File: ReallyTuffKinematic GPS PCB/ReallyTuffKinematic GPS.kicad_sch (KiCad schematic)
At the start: 71 parts, among them IC1 PNT-SG3FS-TR, J1 Conn_01x05_Pin, J2 Conn_01x06_Pin, SW2 SKRPACE010, SW3 SKRPACE010, U1 ESP32-C3-MINI-1-N4, U2 TP4056-42-ESOP8, U3 AP2112K-3.3, U4 DW03C_C41367942, X1 X322512MSB4SI

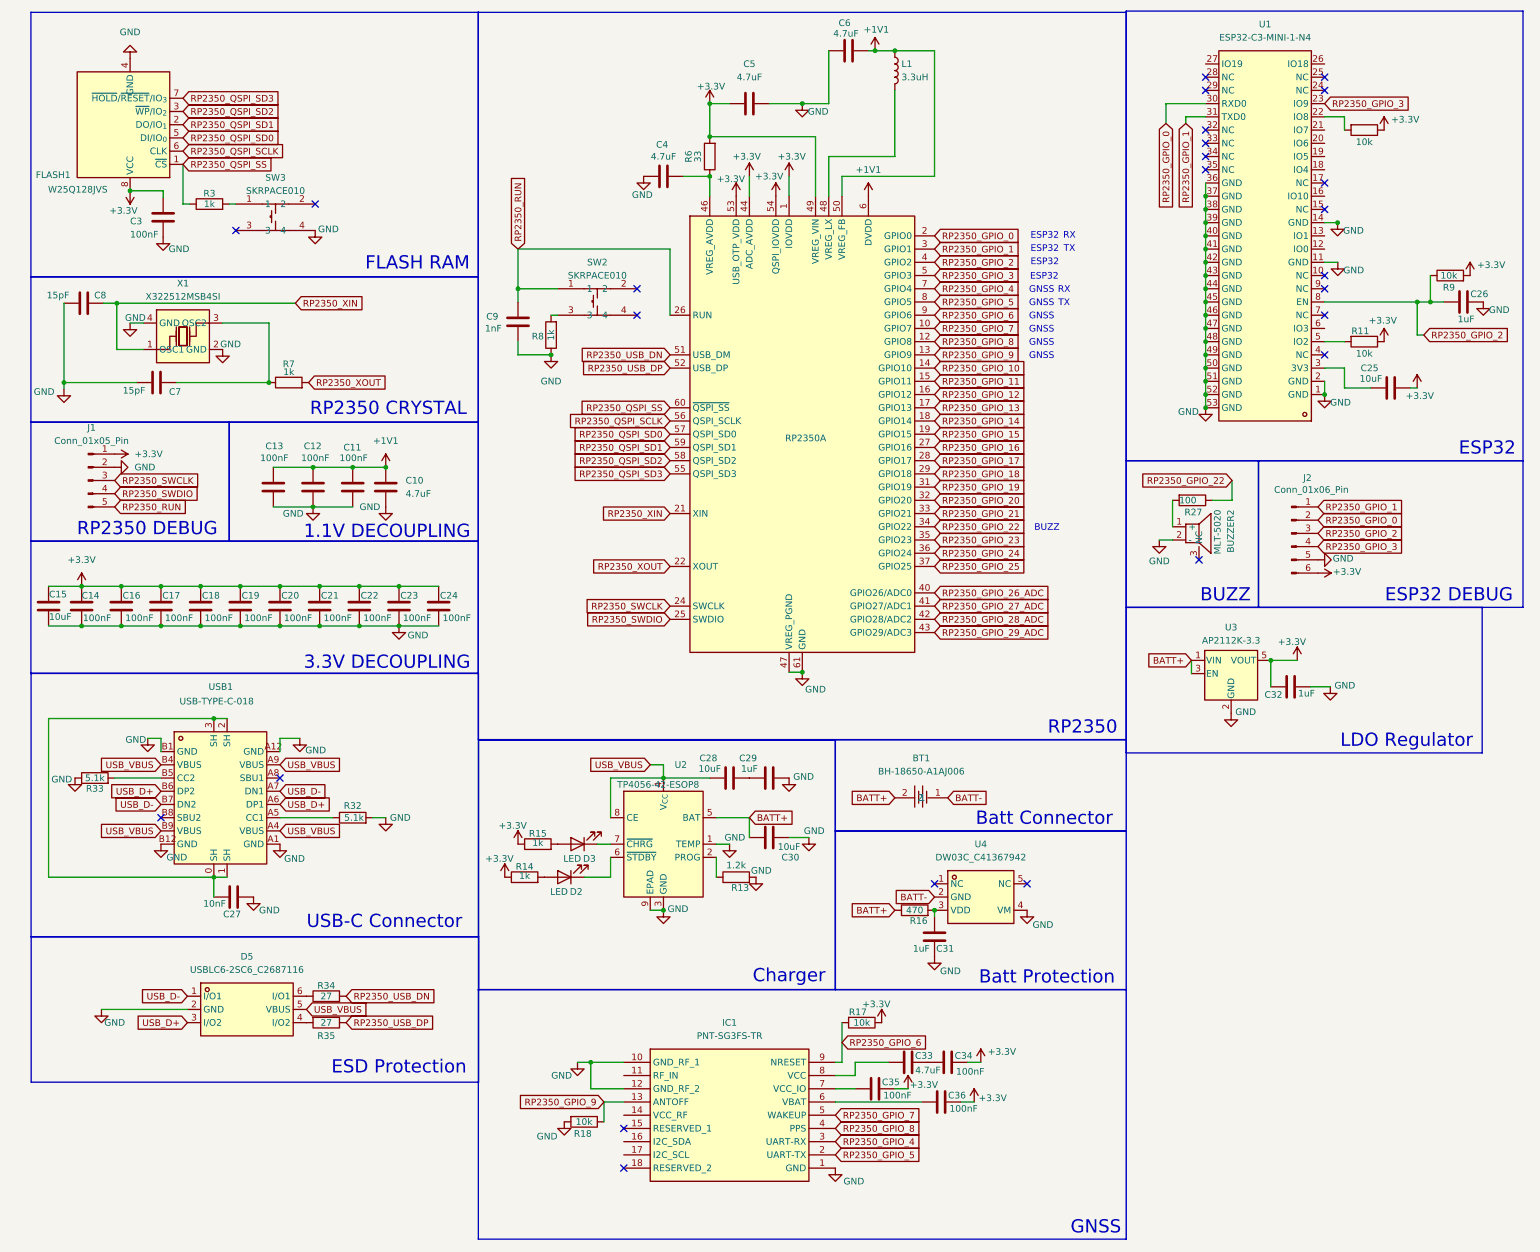
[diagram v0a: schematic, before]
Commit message: began redoing wiring
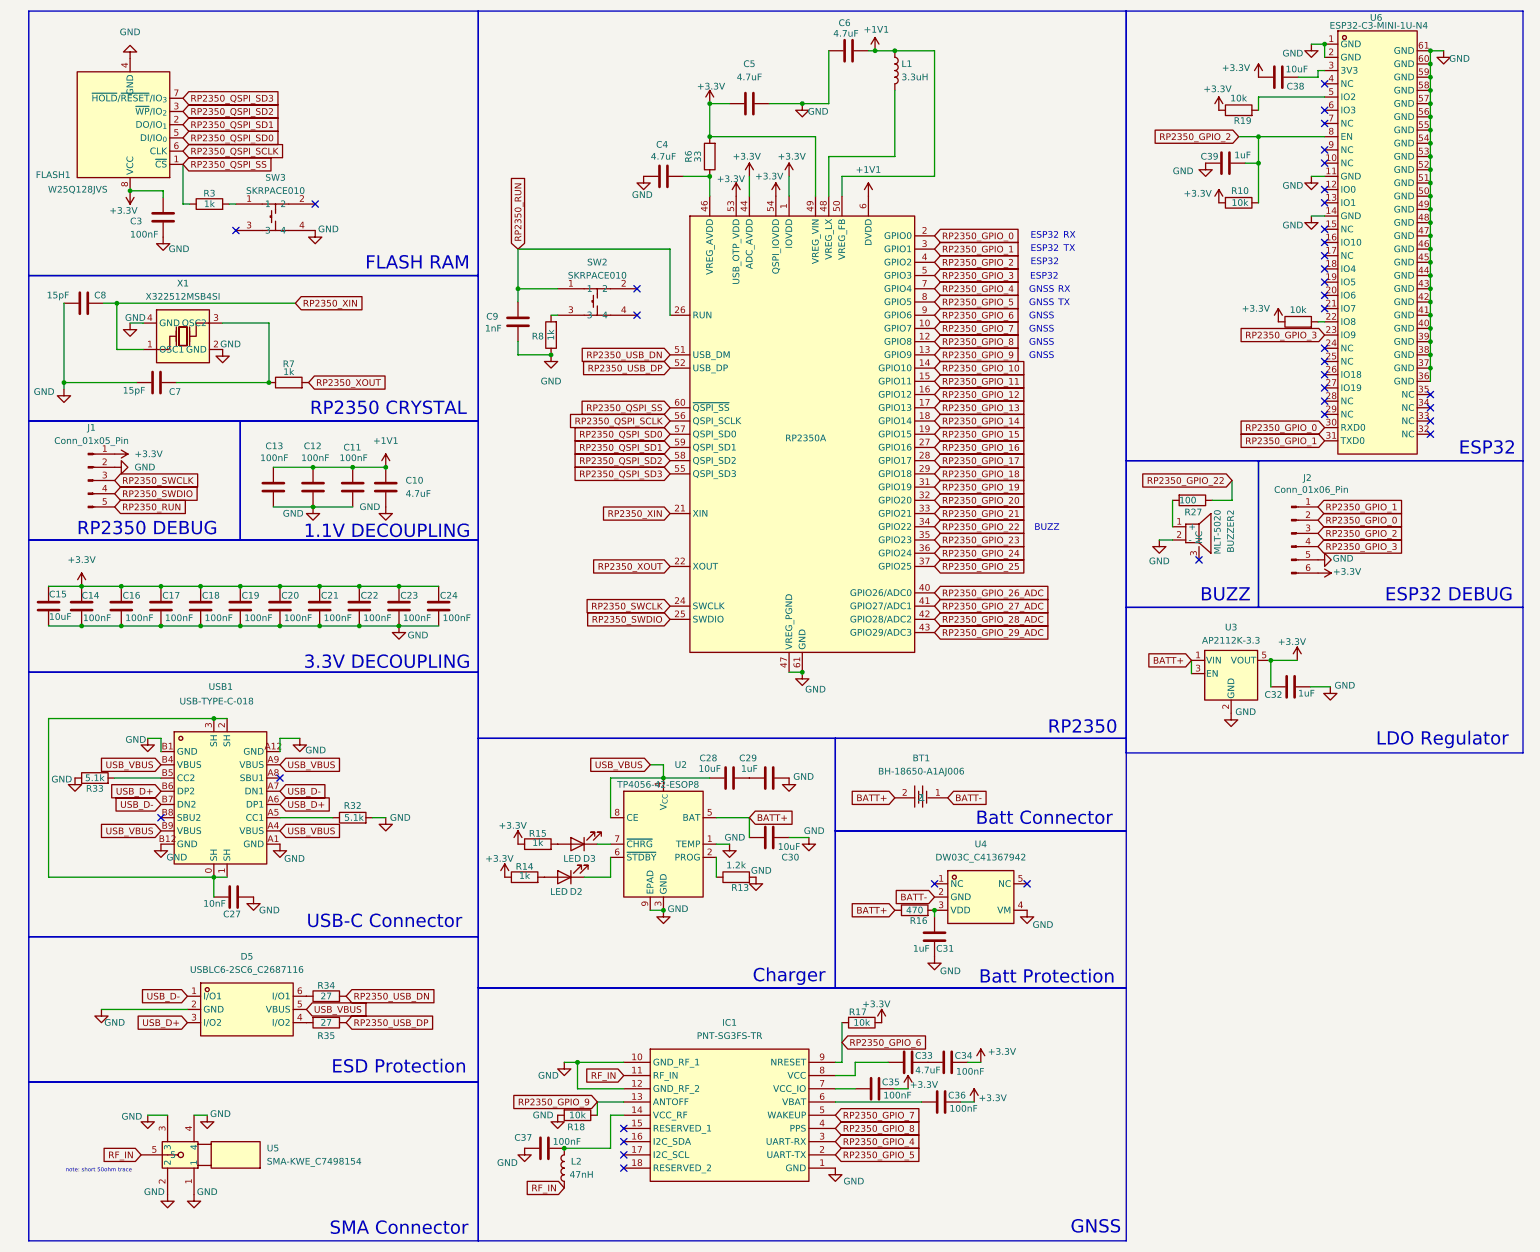
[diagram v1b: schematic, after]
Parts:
- removed C25: 10uF, Capacitor_SMD:C_0603_1608Metric, symbol Device:C
- removed C26: 1uF, Capacitor_SMD:C_0603_1608Metric, symbol Device:C
- removed R11, R12, R9: 10k, Resistor_SMD:R_0603_1608Metric, symbol Device:R
- removed U1: ESP32-C3-MINI-1-N4, easyeda2kicad:WIFIM-SMD_ESP32-C3-MINI-1, symbol easyeda2kicad:ESP32-C3-MINI-1-N4
- added C37: 100nF, Capacitor_SMD:C_0603_1608Metric, symbol Device:C
- added C38: 10uF, Capacitor_SMD:C_0603_1608Metric, symbol Device:C
- added C39: 1uF, Capacitor_SMD:C_0603_1608Metric, symbol Device:C
- added L2: 47nH, symbol Device:L
- added R10, R19, R20: 10k, Resistor_SMD:R_0603_1608Metric, symbol Device:R
- added U5: SMA-KWE_C7498154, easyeda2kicad:SMA-TH_SMA-KWE_C7498154, symbol easyeda2kicad:SMA-KWE_C7498154
- added U6: ESP32-C3-MINI-1U-N4, easyeda2kicad:WIFIM-SMD_61P-L13.2-W12.5-P0.80, symbol easyeda2kicad:ESP32-C3-MINI-1U-N4
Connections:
- net +3.3V: now also C38.2, R10.2, R19.1, R20.1
- net GND: now also C37.1, C39.1, U5.1, U5.2, U5.3, U5.4, U6.1 (GND), U6.11 (GND), U6.14 (GND), U6.2 (GND), U6.36 (GND), U6.37 (GND), U6.38 (GND), U6.39 (GND), U6.40 (GND), U6.41 (GND), U6.42 (GND), U6.43 (GND), U6.44 (GND), U6.45 (GND), U6.46 (GND), U6.47 (GND), U6.48 (GND), U6.49 (GND), U6.50 (GND), U6.51 (GND), U6.52 (GND), U6.53 (GND), U6.54 (GND), U6.55 (GND), U6.56 (GND), U6.57 (GND), U6.58 (GND), U6.59 (GND), U6.60 (GND), U6.61 (GND)
- net RP2350_GPIO_0: now also U6.30 (RXD0)
- net RP2350_GPIO_1: now also U6.31 (TXD0)
- net RP2350_GPIO_2: now also C39.2, R10.1, U6.8 (EN)
- net RP2350_GPIO_3: now also U6.23 (IO9)
- net RF_IN: now reaches IC1.11 (RF_IN)
- net RF_IN: now also L2.1, U5.5
- net at IC1.14 (VCC_RF): now also C37.2, L2.2
- new net: C38.1, U6.3 (3V3)
- new net: R20.2, U6.22 (IO8)
- new net: R19.2, U6.5 (IO2)
- no-connect marks 25 -> 37
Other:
- note added: "SMA Connector"
- note added: "note: short 50ohm trace"
- moved on the sheet: R18
